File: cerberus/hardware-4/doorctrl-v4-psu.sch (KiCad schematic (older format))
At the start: 30 parts, among them U2 MC34063, U3 L4960

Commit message: Various fiddeling
git-svn-id: file:///home/ff/projects/osaa/svn@243 a092026d-3e22-4cff-94a7-eaa6fdd35d37
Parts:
- C16: value 100nF -> 10uF
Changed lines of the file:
@@
-EESchema Schematic File Version 2  date 2011-01-03T13:24:02 CET
+EESchema Schematic File Version 2  date 2011-01-03T16:40:54 CET
 LIBS:enc28j60
 LIBS:power
@@
 P 5150 4900
 F 0 "C16" H 5200 5000 50  0000 L CNN
-F 1 "100nF" H 5200 4800 50  0000 L CNN
+F 1 "10uF" H 5200 4800 50  0000 L CNN
 	1    5150 4900
 	1    0    0    -1

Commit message: Various cleanups
git-svn-id: file:///home/ff/projects/osaa/svn@255 a092026d-3e22-4cff-94a7-eaa6fdd35d37
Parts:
- C10: value 1200uF -> 1000uF/35V
- C15: value 100uF -> 220uF
- C16: value 10uF -> 100nF
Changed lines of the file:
@@
-EESchema Schematic File Version 2  date 2011-01-03T16:40:54 CET
+EESchema Schematic File Version 2  date 2011-01-17T19:42:11 CET
 LIBS:enc28j60
 LIBS:power
@@
 Sheet 6 6
 Title ""
-Date "3 jan 2011"
+Date "17 jan 2011"
 Rev ""
 Comp ""
@@
 P 5150 4900
 F 0 "C16" H 5200 5000 50  0000 L CNN
-F 1 "10uF" H 5200 4800 50  0000 L CNN
+F 1 "100nF" H 5200 4800 50  0000 L CNN
 	1    5150 4900
 	1    0    0    -1
@@
 P 2200 4900
 F 0 "C10" H 2050 5000 50  0000 L CNN
-F 1 "1200uF" H 1900 4800 50  0000 L CNN
+F 1 "1000uF/35V" H 1900 4800 50  0000 L CNN
 	1    2200 4900
 	1    0    0    -1
@@
 P 5050 2800
 F 0 "C15" H 5100 2900 50  0000 L CNN
-F 1 "100uF" H 5100 2700 50  0000 L CNN
+F 1 "220uF" H 5100 2700 50  0000 L CNN
 	1    5050 2800
 	1    0    0    -1

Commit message: Misc price cleanup
git-svn-id: file:///home/ff/projects/osaa/svn@256 a092026d-3e22-4cff-94a7-eaa6fdd35d37
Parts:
- C14: value 1000uF -> 1000uF/35V
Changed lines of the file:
@@
-EESchema Schematic File Version 2  date 2011-01-17T19:42:11 CET
+EESchema Schematic File Version 2  date 2011-01-17T20:19:18 CET
 LIBS:enc28j60
 LIBS:power
@@
 P 4800 4900
 F 0 "C14" H 4650 5000 50  0000 L CNN
-F 1 "1000uF" H 4500 4800 50  0000 L CNN
+F 1 "1000uF/35V" H 4450 4650 50  0000 L CNN
 	1    4800 4900
 	1    0    0    -1
@@
 P 2200 4900
 F 0 "C10" H 2050 5000 50  0000 L CNN
-F 1 "1000uF/35V" H 1900 4800 50  0000 L CNN
+F 1 "1000uF/35V" H 1900 4650 50  0000 L CNN
 	1    2200 4900
 	1    0    0    -1

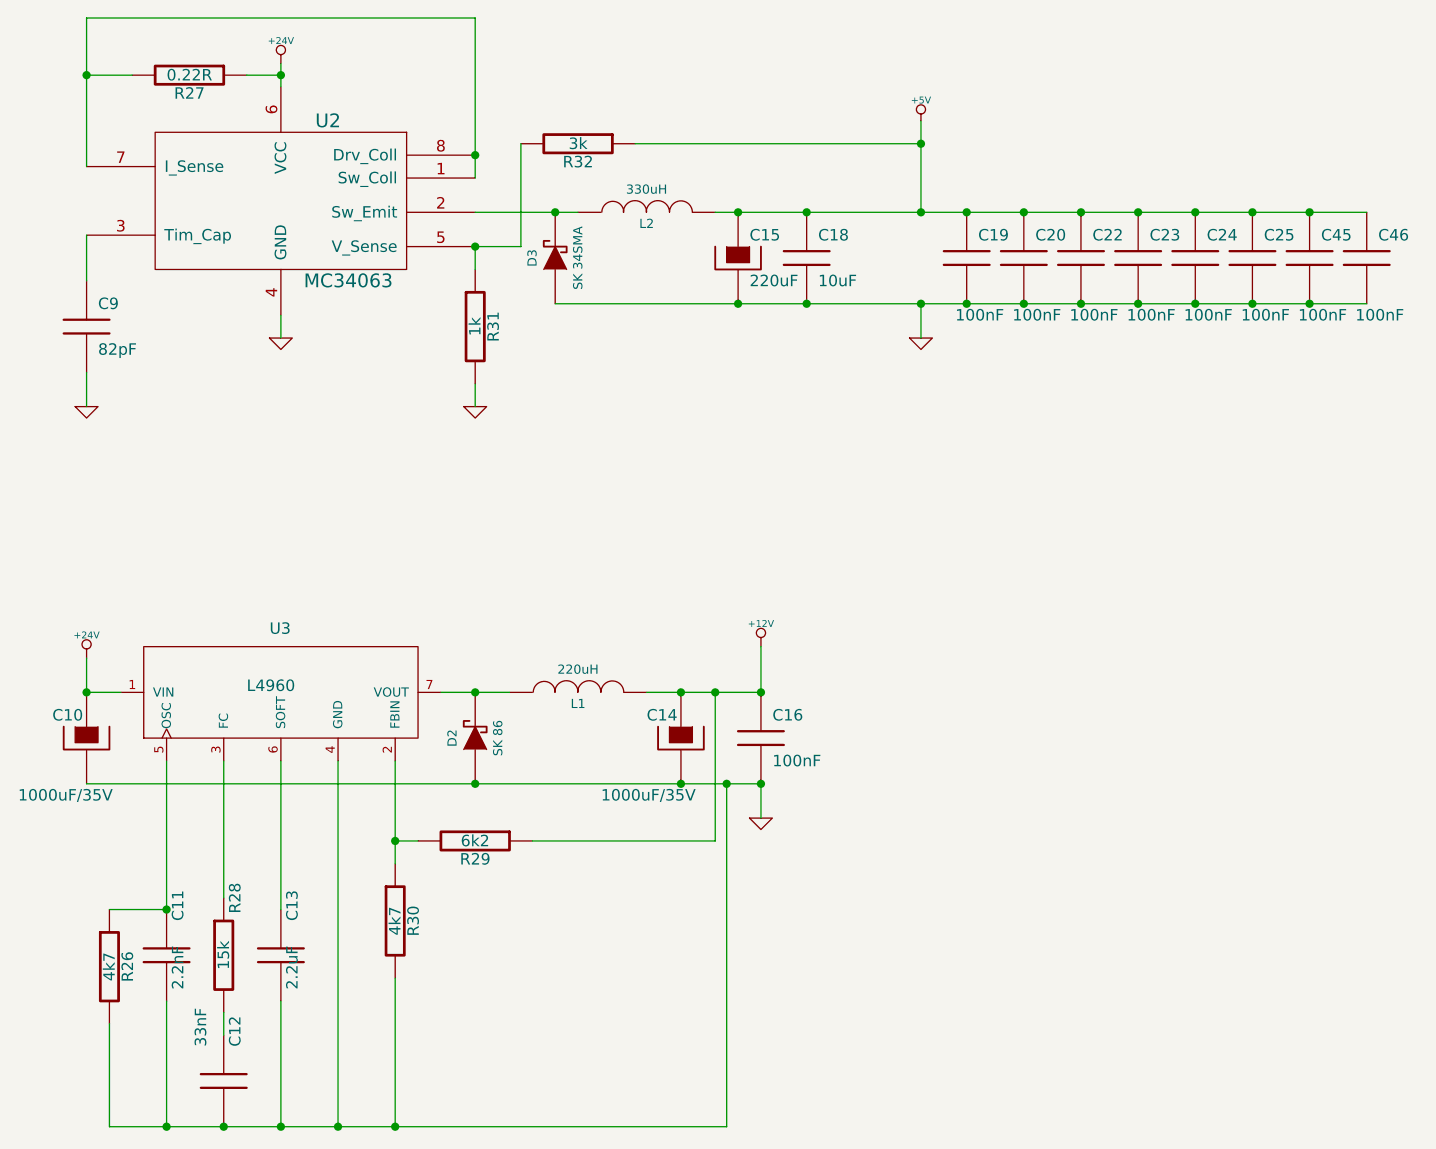
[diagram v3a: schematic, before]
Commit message: Fixed a couple of bugs: No more level shifter and rfid carrier wave output is connected correctly
git-svn-id: file:///home/ff/projects/osaa/svn@258 a092026d-3e22-4cff-94a7-eaa6fdd35d37
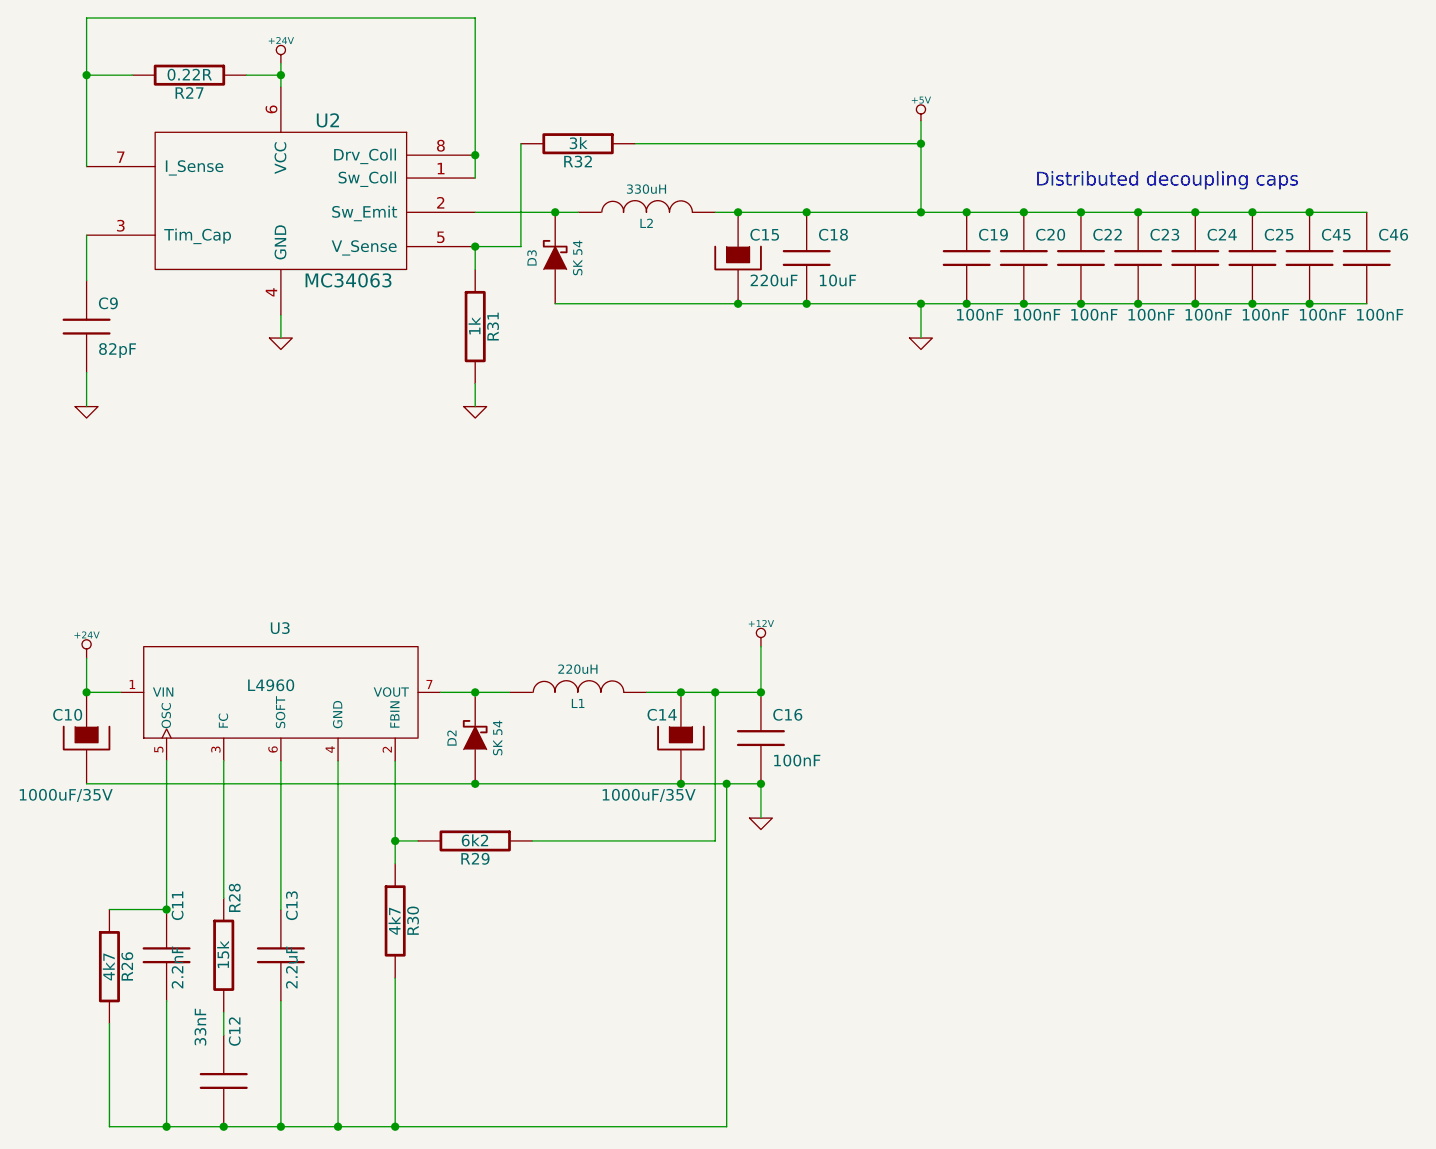
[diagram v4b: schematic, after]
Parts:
- D2: value SK 86 -> SK 54
- D3: value SK 34SMA -> SK 54
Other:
- note added: "Distributed decoupling caps"
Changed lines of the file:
@@
-EESchema Schematic File Version 2  date 2011-01-17T20:19:18 CET
+EESchema Schematic File Version 2  date 2011-01-23T22:09:23 CET
 LIBS:enc28j60
 LIBS:power
@@
 Sheet 6 6
 Title ""
-Date "17 jan 2011"
+Date "23 jan 2011"
 Rev ""
 Comp ""
@@
 Comment4 ""
 $EndDescr
+Text Notes 6350 2500 0    60   ~ 0
+Distributed decoupling caps
 Wire Wire Line
 	7800 2600 4950 2600
@@
 P 3900 4900
 F 0 "D2" H 3900 5000 40  0000 C CNN
-F 1 "SK 86" H 3900 4800 40  0000 C CNN
+F 1 "SK 54" H 3900 4800 40  0000 C CNN
 	1    3900 4900
 	0    -1   -1   0
@@
 P 4250 2800
 F 0 "D3" H 4250 2900 40  0000 C CNN
-F 1 "SK 34SMA" H 4250 2700 40  0000 C CNN
+F 1 "SK 54" H 4250 2700 40  0000 C CNN
 	1    4250 2800
 	0    -1   -1   0
